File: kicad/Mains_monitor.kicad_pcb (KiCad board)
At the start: 2 copper layers, 99.5 x 99.5 mm, 31 parts, among them J1 Screw_Terminal_01x02, J2 Screw_Terminal_01x02, K1 SANYOU_SRD_Form_C, Q1 NPN, U1 HLW8032

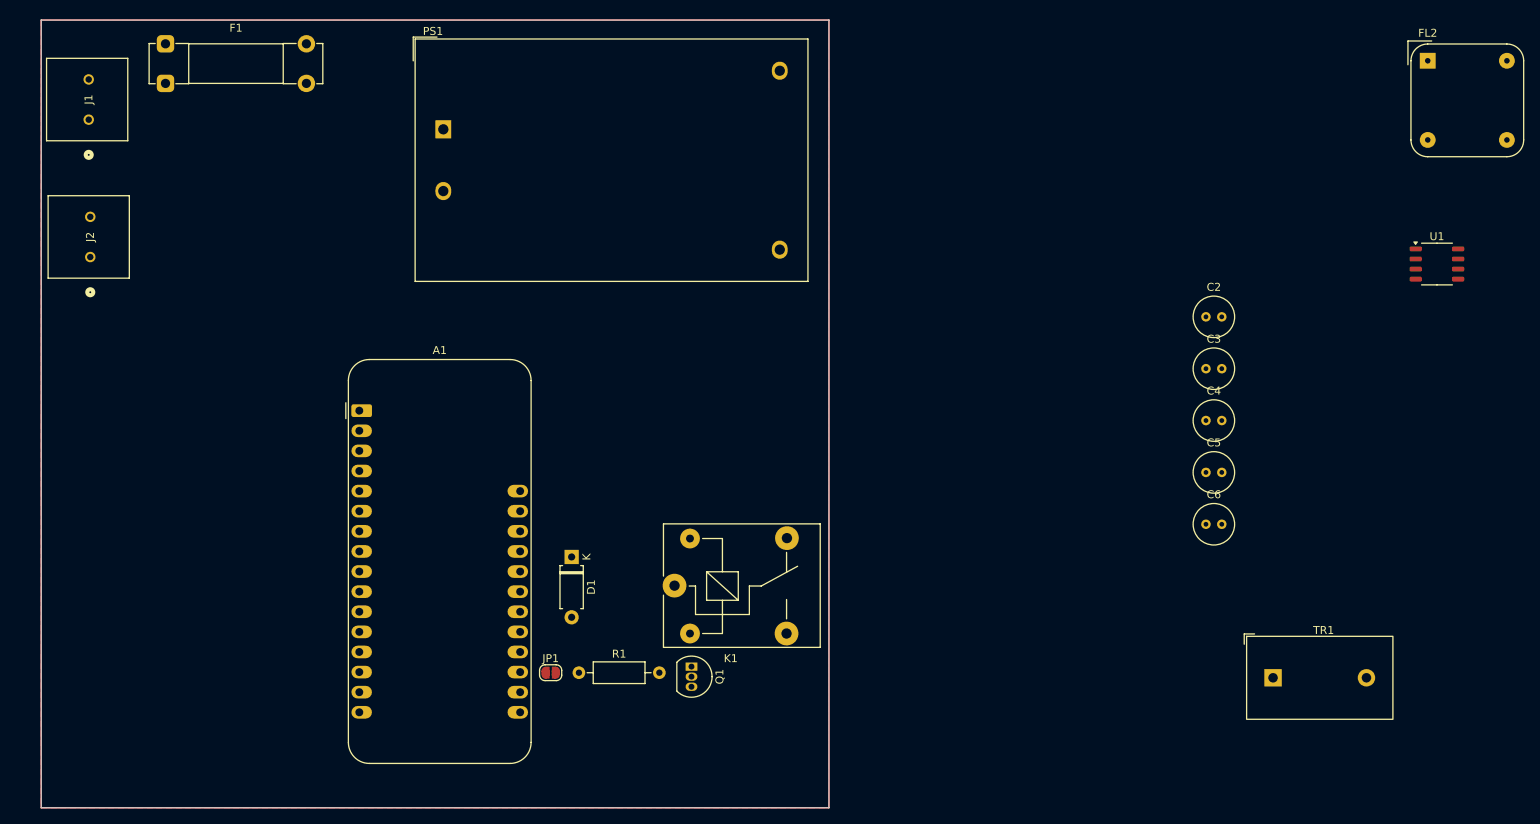
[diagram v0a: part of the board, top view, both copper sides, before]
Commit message: added mounting holes and ground layers
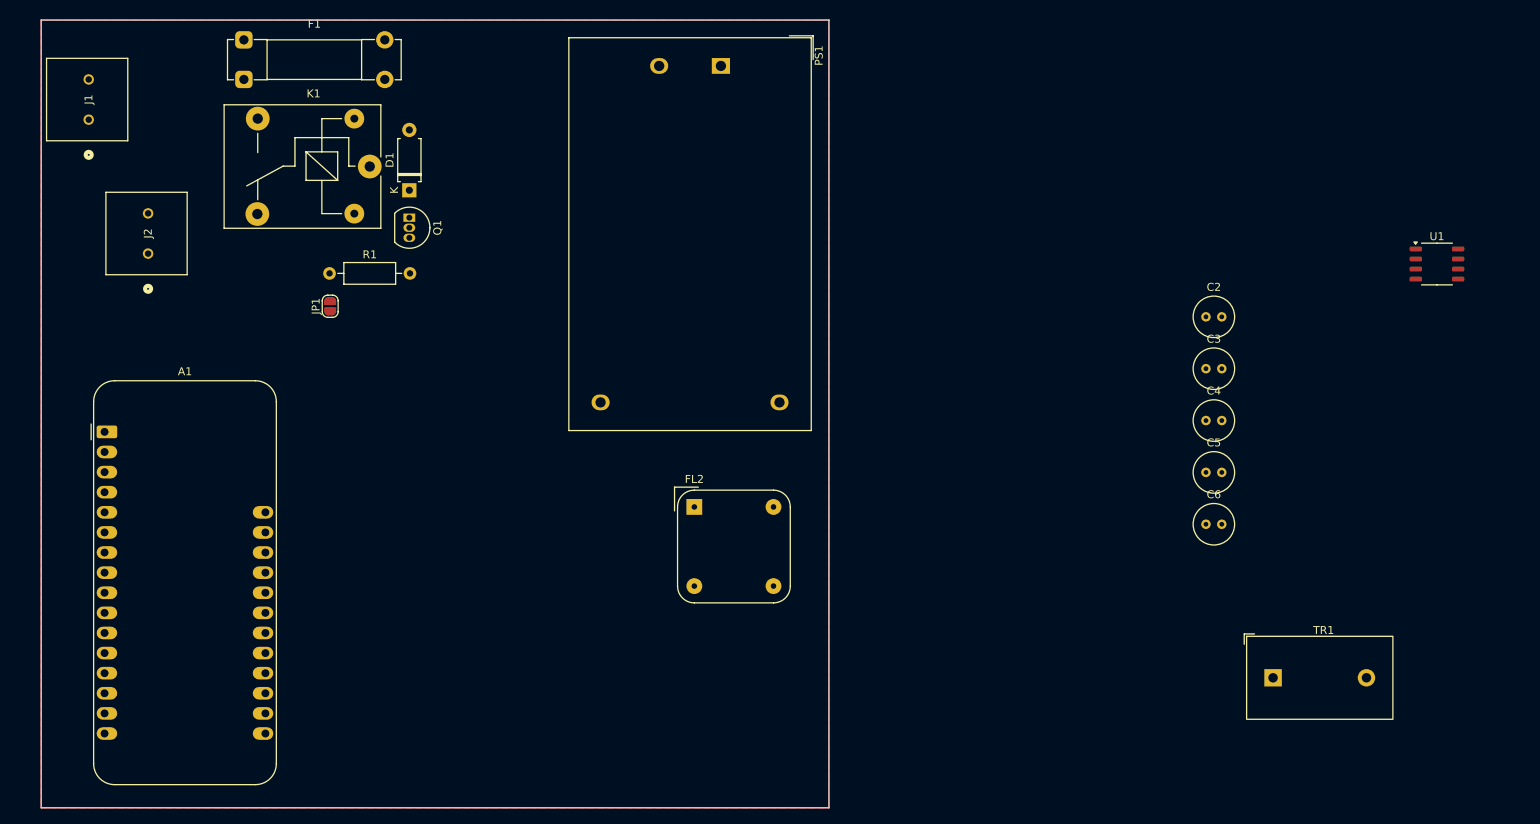
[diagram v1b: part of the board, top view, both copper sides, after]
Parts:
- moved FL2 108.4 mm to (173.0, 106.5)
- moved Q1 67.0 mm to (137.0, 70.0)
- moved K1 65.5 mm to (132.0, 63.5), turned to 180 degrees
- moved R1 59.5 mm to (126.9, 77.0)
- moved JP1 54.0 mm to (127.0, 81.2), turned to 90 degrees
- moved D1 50.7 mm to (137.0, 66.5), turned to 90 degrees
- moved PS1 36.0 mm to (176.4, 50.8), turned to -90 degrees
- moved A1 32.3 mm to (98.5, 97.0)
- moved F1 9.91 mm to (116.1, 47.5)
- moved J2 7.32 mm to (104.0, 74.5)

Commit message: PCB layout updated, traces and base fill added, still need to make space for mounting holes
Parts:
- added H1: MountingHole, MountingHole:MountingHole_5.3mm_M5, F.Cu at (60.5, 61.5)
- added H2: MountingHole, MountingHole:MountingHole_5.3mm_M5, F.Cu at (60.5, 73.7)
- added H3: MountingHole, MountingHole:MountingHole_5.3mm_M5, F.Cu at (60.5, 85.8)
- added H4: MountingHole, MountingHole:MountingHole_5.3mm_M5, F.Cu at (60.5, 98.0)
- moved U1 161.3 mm to (118.0, 138.1)
- moved C6 133.4 mm to (108.0, 140.0)
- moved TR1 131.4 mm to (115.7, 111.6)
- moved C3 125.5 mm to (118.5, 128.5), turned to 180 degrees
- moved R2 122.0 mm to (126.5, 122.0), turned to 180 degrees
- moved R3 120.9 mm to (129.5, 119.9), turned to -90 degrees
- moved C2 120.7 mm to (126.0, 128.5), turned to 180 degrees
- moved R8 117.1 mm to (123.9, 141.5)
- moved R10 109.4 mm to (123.9, 135.5)
- moved R4 105.1 mm to (113.0, 119.9), turned to -90 degrees
- moved R7 92.8 mm to (93.9, 135.0)
- moved R9 91.3 mm to (93.9, 141.0)
- moved C5 84.7 mm to (153.5, 92.0)
- moved C4 83.1 mm to (155.5, 83.0), turned to 180 degrees
- moved FL2 79.6 mm to (94.1, 117.6)
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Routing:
- net +5V: track 0.00 -> 171.8 mm
- net AC_N: track 0.00 -> 91.5 mm
- net /RLY_CTRL: track 0.00 -> 66.6 mm
- net RELAY_OUT: track 0.00 -> 66.4 mm
- net AC_H: track 0.00 -> 64.3 mm
- net /DATA_LV: track 0.00 -> 44.1 mm
- net Net-(J1-Pin_2): track 0.00 -> 27.1 mm
- net IP: track 0.00 -> 21.4 mm
- net Net-(FL2-Pad4): track 0.00 -> 20.0 mm
- net Net-(D1-A): track 0.00 -> 16.6 mm
- net IN: track 0.00 -> 13.9 mm
- net Net-(R2-Pad1): track 0.00 -> 13.0 mm
- net VP: track 0.00 -> 12.6 mm
- net /DATA_HV: track 0.00 -> 10.4 mm
- net Net-(Q1-B): track 0.00 -> 8.83 mm
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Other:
- board text added: "H_in"
- board text added: "H_out"
- board text added: "N_in"
- board text added: "N_out"

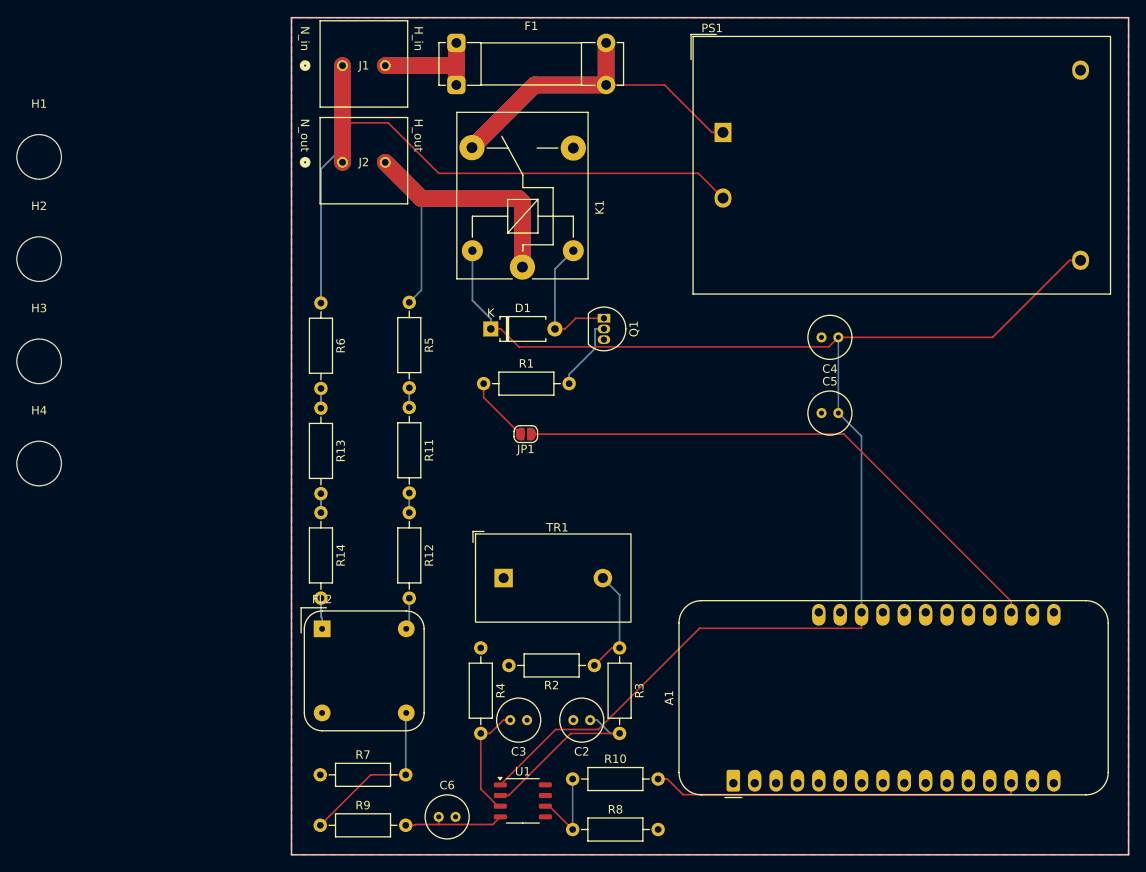
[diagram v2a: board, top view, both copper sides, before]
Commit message: added net class for 120V and mounting holes
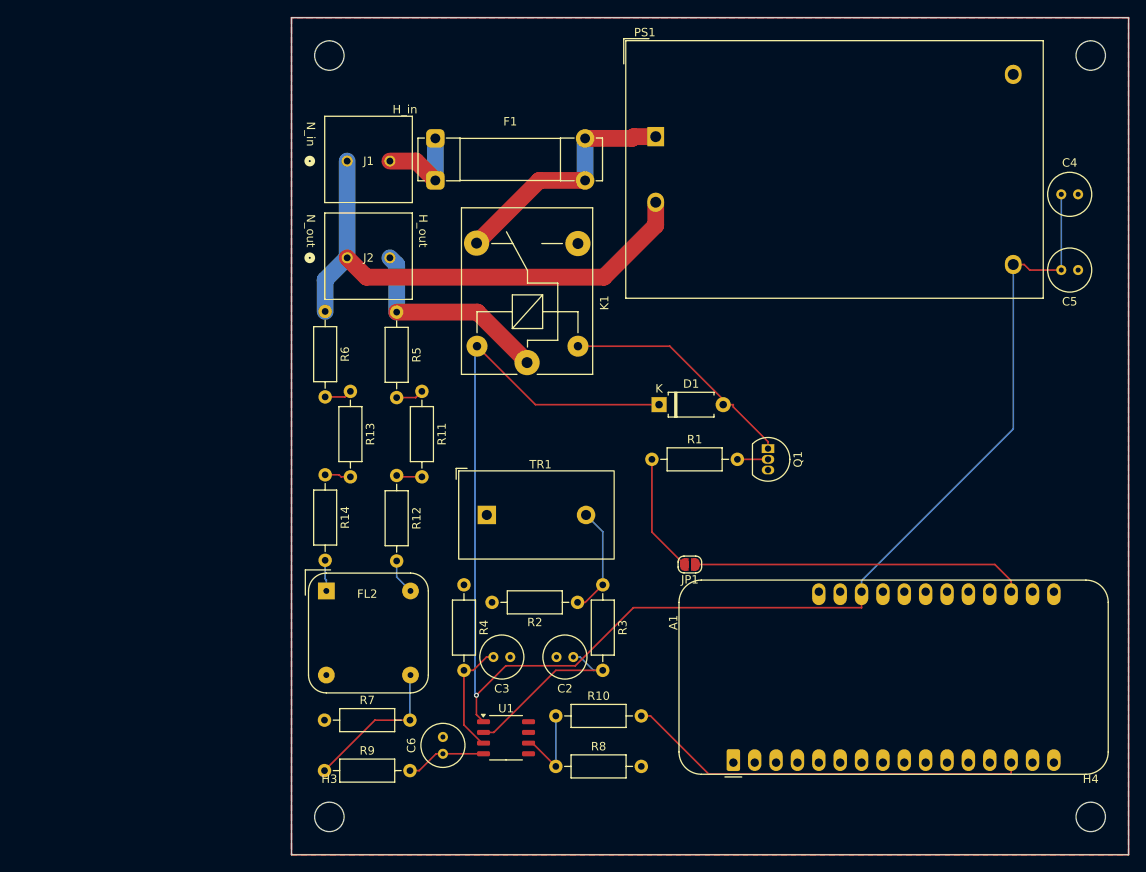
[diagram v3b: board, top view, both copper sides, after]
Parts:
- H1, H2, H3, H4: footprint MountingHole:MountingHole_5.3mm_M5 -> MountingHole:MountingHole_3.5mm
- moved H4 131.9 mm to (185.5, 140.0)
- moved H2 127.3 mm to (185.5, 49.5)
- moved H3 64.2 mm to (95.0, 140.0)
- moved H1 36.5 mm to (95.0, 49.5)
- moved C5 34.9 mm to (184.0, 75.0), turned to 180 degrees
- moved C4 31.5 mm to (182.0, 66.0), turned to 0 degrees
- moved JP1 24.9 mm to (137.8, 110.0)
- moved Q1 24.9 mm to (147.1, 96.2)
- moved D1 21.9 mm to (134.2, 91.0)
- moved R1 21.9 mm to (133.3, 97.5)
- moved F1 11.6 mm to (107.6, 59.4)
- moved J1 11.4 mm to (97.1, 62.0)
- moved J2 11.4 mm to (97.1, 73.5)
- moved K1 11.4 mm to (118.5, 86.0)
- moved PS1 8.02 mm to (133.8, 59.1)
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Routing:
- net RELAY_OUT: track 66.4 -> 24.8 mm
- net AC_H: track 64.3 -> 29.5 mm
- net AC_N: track 91.5 -> 61.9 mm
- net /RLY_CTRL: track 66.6 -> 39.6 mm
- net Net-(J1-Pin_2): track 27.1 -> 11.4 mm
- net Net-(D1-A): track 16.6 -> 28.9 mm
- net +5V: track 171.8 -> 183.0 mm, vias 0 -> 1
- net Net-(JP1-B): track 7.81 -> 14.1 mm
- net Net-(Q1-B): track 8.83 -> 3.64 mm
- net /DATA_LV: track 44.1 -> 48.1 mm
- net VP: track 12.6 -> 9.57 mm
- net Net-(FL2-Pad4): track 20.0 -> 18.0 mm
- net Net-(R11-Pad1): track 2.34 -> 3.31 mm
- net Net-(R13-Pad1): track 2.34 -> 3.27 mm
- net Net-(R13-Pad2): track 2.26 -> 3.10 mm
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
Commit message: backup files
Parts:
- moved C4 68.0 mm to (120.0, 94.0), turned to -90 degrees
- moved C5 61.5 mm to (125.5, 94.0), turned to 90 degrees
- moved R4 35.9 mm to (138.0, 136.1), turned to 90 degrees
- moved A1 35.5 mm to (153.1, 99.4), turned to -90 degrees
- moved TR1 32.9 mm to (102.7, 135.1)
- moved JP1 31.0 mm to (110.5, 95.3), turned to 90 degrees
- moved Q1 25.7 mm to (123.6, 85.7)
- moved R3 24.4 mm to (121.5, 136.1), turned to 90 degrees
- moved R1 24.0 mm to (110.4, 90.5)
- moved D1 23.8 mm to (110.7, 87.0)
- moved R10 22.2 mm to (124.9, 106.0)
- moved R8 22.2 mm to (124.9, 112.0)
- moved H4 21.6 mm to (164.0, 137.5)
- moved H2 21.5 mm to (164.0, 49.5)
- moved U1 20.8 mm to (119.0, 110.0)
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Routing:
- net +5V: track 183.0 -> 84.1 mm, vias 1 -> 0
- net AC_H: track 29.5 -> 72.5 mm
- net /DATA_LV: track 48.1 -> 18.9 mm
- net RELAY_OUT: track 24.8 -> 47.7 mm
- net IN: track 13.9 -> 34.0 mm, vias 0 -> 1
- net AC_N: track 61.9 -> 81.7 mm
- net Net-(D1-A): track 28.9 -> 12.6 mm
- net VP: track 9.57 -> 23.0 mm
- net /RLY_CTRL: track 39.6 -> 28.7 mm
- net Net-(J1-Pin_2): track 11.4 -> 22.0 mm
- net Net-(JP1-B): track 14.1 -> 4.23 mm
- net IP: track 21.4 -> 26.3 mm
- net Net-(FL2-Pad4): track 18.0 -> 15.3 mm
- net Net-(Q1-B): track 3.64 -> 5.38 mm
- net Net-(R2-Pad1): track 13.0 -> 11.2 mm
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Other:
- board size 99.5 x 99.5 mm -> 78 x 97 mm

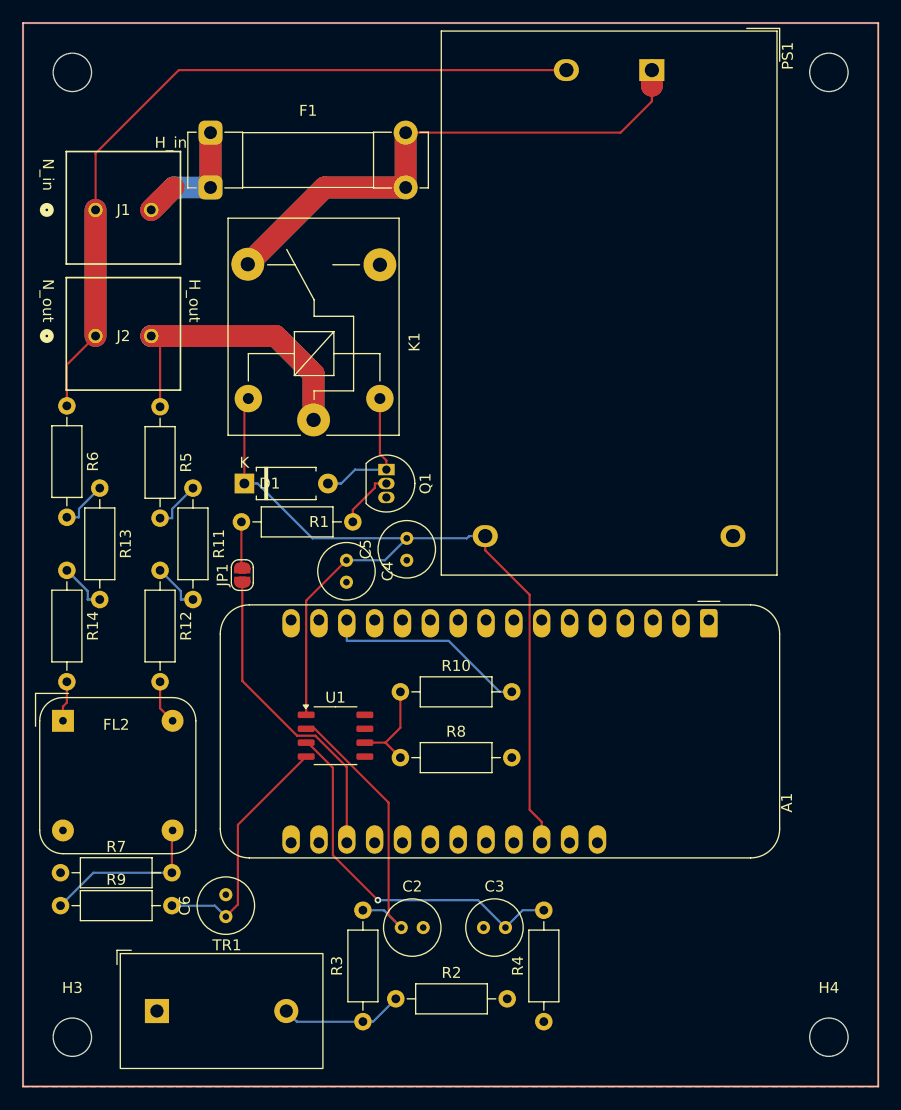
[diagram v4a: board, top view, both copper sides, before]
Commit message: Updated PCB layout with new components, decreased board size
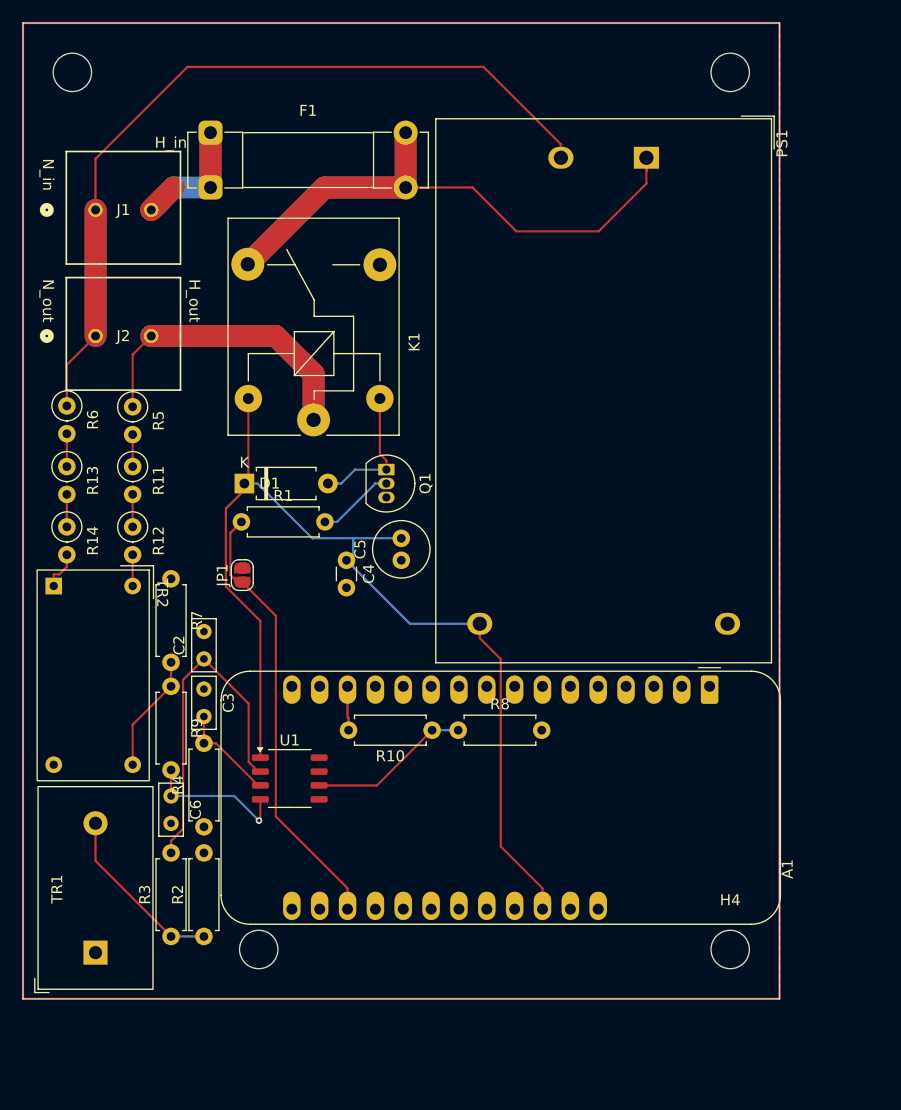
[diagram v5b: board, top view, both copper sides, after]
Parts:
- C2, C3, C6: footprint Capacitor_THT:C_Radial_D5.0mm_H7.0mm_P2.00mm -> Capacitor_THT:C_Rect_L4.6mm_W2.0mm_P2.50mm_MKS02_FKP02
- C4: footprint Capacitor_THT:C_Radial_D5.0mm_H7.0mm_P2.00mm -> Capacitor_THT:C_Disc_D3.0mm_W1.6mm_P2.50mm
- C5: footprint Capacitor_THT:C_Radial_D5.0mm_H7.0mm_P2.00mm -> Capacitor_THT:C_Radial_D5.0mm_H11.0mm_P2.00mm
- R1, R10, R2, R3, R4, R7, R8, R9: footprint Resistor_THT:R_Axial_DIN0207_L6.3mm_D2.5mm_P10.16mm_Horizontal -> Resistor_THT:R_Axial_DIN0207_L6.3mm_D2.5mm_P7.62mm_Horizontal
- R11, R12, R13, R14, R5, R6: footprint Resistor_THT:R_Axial_DIN0207_L6.3mm_D2.5mm_P10.16mm_Horizontal -> Resistor_THT:R_Axial_DIN0207_L6.3mm_D2.5mm_P2.54mm_Vertical
- TR2: renamed from FL2; value choke -> ZMPT107; footprint Inductor_THT:Choke_Schaffner_RN102-04-14.0x14.0mm -> mains_mon:ZMPT107-1
- moved R4 35.7 mm to (107.0, 118.3)
- moved C3 33.5 mm to (107.0, 105.8), turned to -90 degrees
- moved C2 30.4 mm to (107.0, 103.0), turned to 90 degrees
- moved R7 28.6 mm to (104.0, 95.7), turned to -90 degrees
- moved R9 22.4 mm to (104.0, 105.5), turned to -90 degrees
- moved R3 19.1 mm to (104.0, 128.3)
- moved H3 18.8 mm to (112.0, 129.5)
- moved R2 18.4 mm to (107.0, 128.3), turned to 90 degrees
- moved C6 12.1 mm to (104.0, 115.5), turned to -90 degrees
- moved H4 12.0 mm to (155.0, 129.5)
- moved H2 9.00 mm to (155.0, 49.5)
- moved PS1 8.02 mm to (147.4, 57.3)
- moved TR1 7.73 mm to (97.1, 129.8), turned to 90 degrees
- moved A1 6.05 mm to (153.1, 105.5)
- moved R11 5.84 mm to (100.5, 85.5)
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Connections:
- R1 pad 1: Net-(JP1-B) -> /RLY_CTRL
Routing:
- net IN: track 34.0 -> 9.18 mm, vias 1 -> 0
- net /DATA_LV: track 18.9 -> 4.04 mm
- net +5V: track 84.1 -> 97.5 mm
- net /RLY_CTRL: track 28.7 -> 40.4 mm
- net VP: track 23.0 -> 13.3 mm, vias 0 -> 1
- net /DATA_HV: track 9.01 -> 14.8 mm
- net IP: track 26.3 -> 31.5 mm
- net Net-(R2-Pad1): track 11.2 -> 16.2 mm
- net Net-(R7-Pad2): track 15.3 -> 10.8 mm
- net Net-(JP1-B): track 4.23 -> 0.00 mm
- net AC_N: track 81.7 -> 85.5 mm
- net Net-(R11-Pad1): track 4.63 -> 2.91 mm
- net Net-(Q1-B): track 5.38 -> 7.08 mm
- net Net-(R13-Pad2): track 4.55 -> 2.96 mm
- net Net-(R11-Pad2): track 4.55 -> 2.96 mm
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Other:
- board size 78 x 97 mm -> 69 x 89 mm
